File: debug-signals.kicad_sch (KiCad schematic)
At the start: 77 parts, among them U11 TCA9534PWR, U12 TCA9534PWR, U13 Si7021, U14 TCA9534PWR, U15 TCA9534PWR

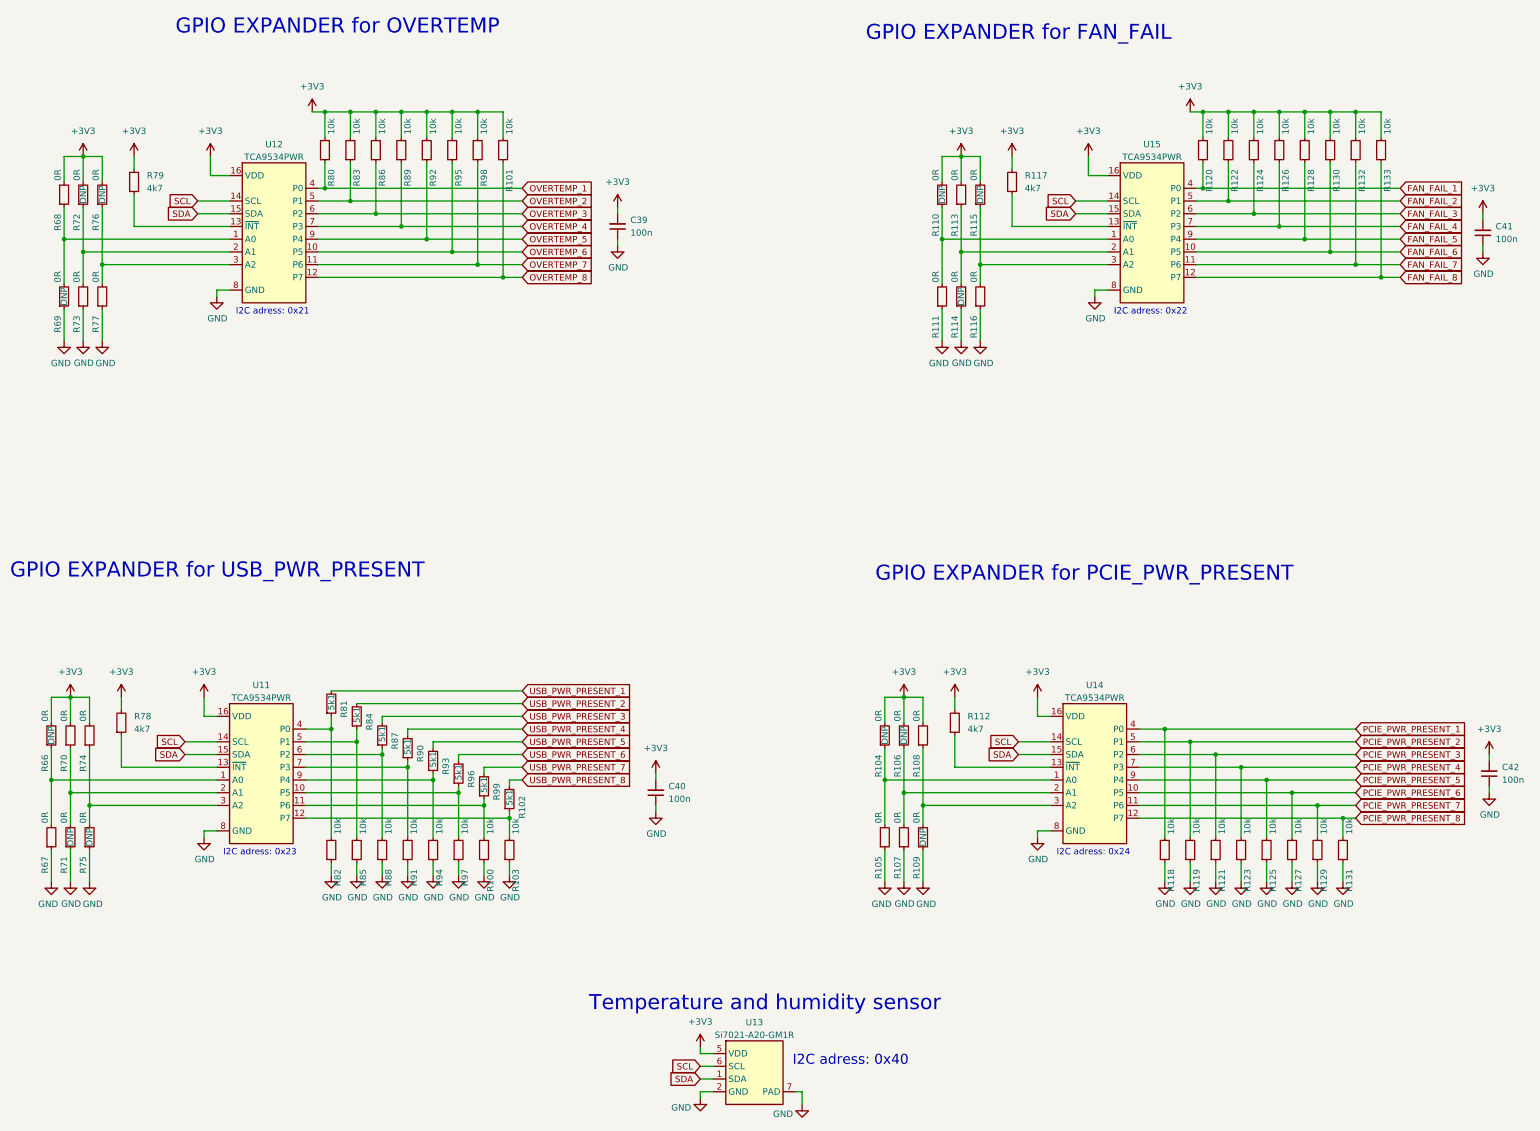
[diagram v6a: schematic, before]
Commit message: Minor fixes in schematic layout and reannotate
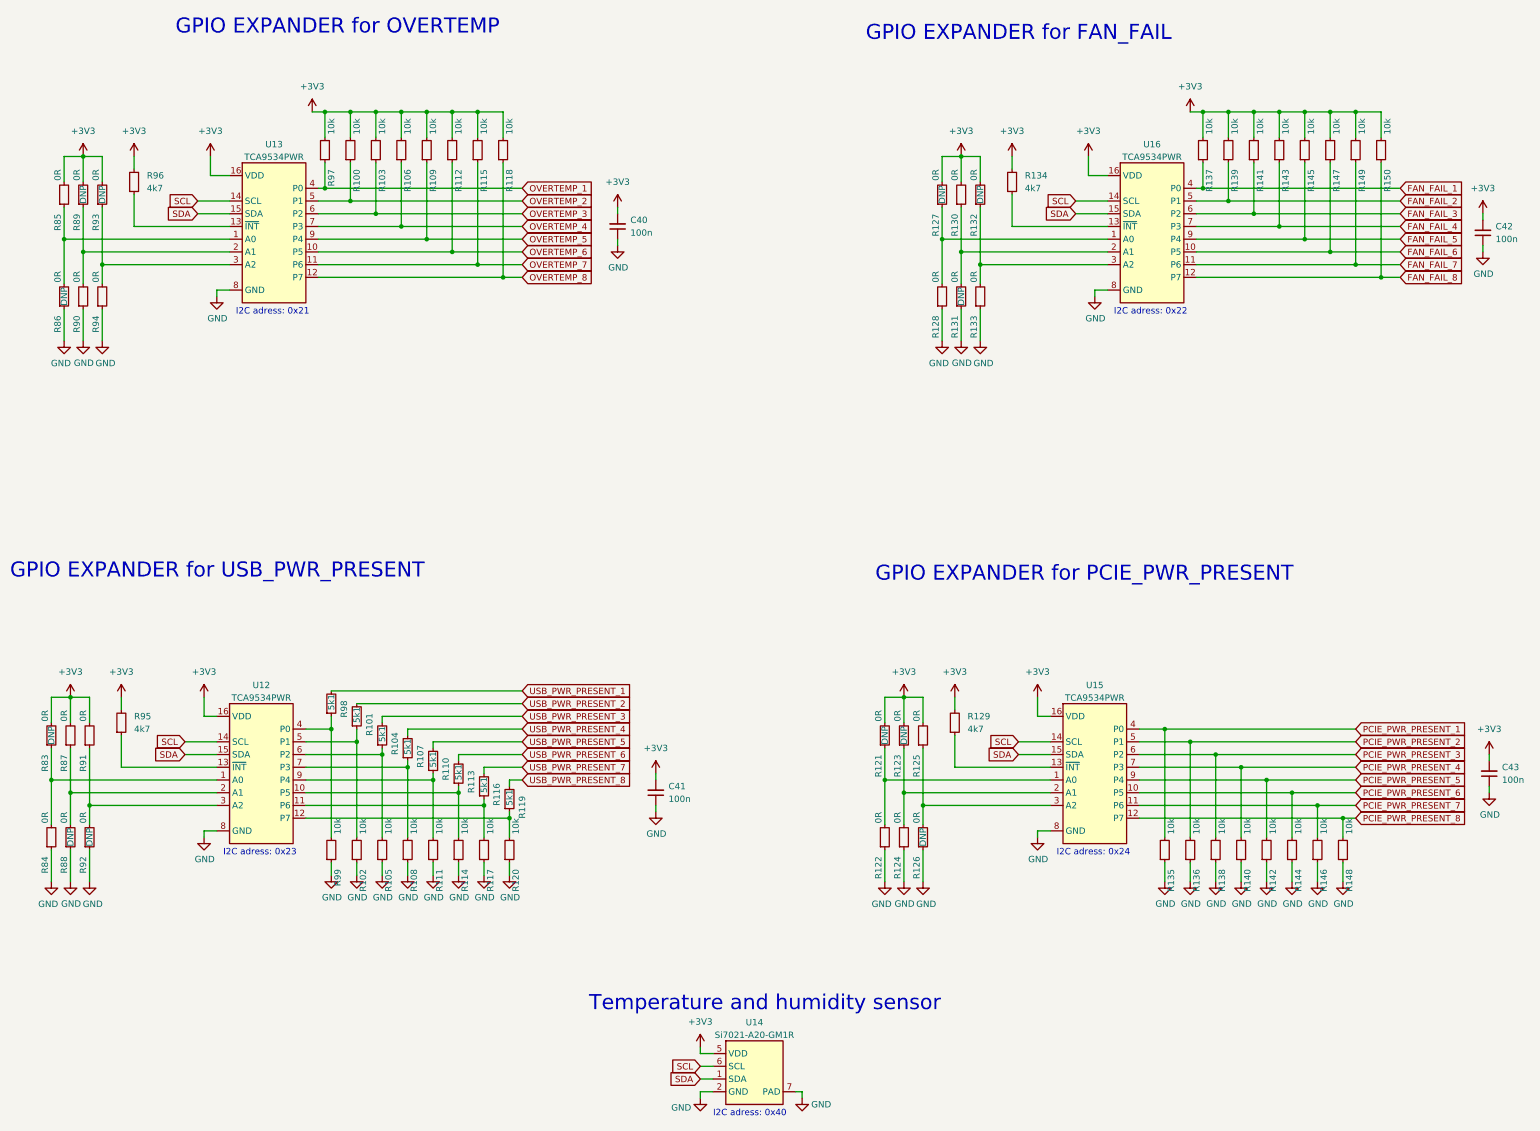
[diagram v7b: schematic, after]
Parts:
- renumbered C39 to C40, C40 to C41, C41 to C42, C42 to C43, R83 to R100, R84 to R101, R85 to R102, R86 to R103, R87 to R104, R88 to R105, R89 to R106, R90 to R107, R91 to R108, R92 to R109, R93 to R110, R94 to R111, R95 to R112, R96 to R113, R97 to R114, R98 to R115, R99 to R116, R100 to R117, R101 to R118, R102 to R119, R103 to R120, R104 to R121, R105 to R122, R106 to R123, R107 to R124, R108 to R125, R109 to R126, R110 to R127, R111 to R128, R112 to R129, R113 to R130, R114 to R131, R115 to R132, R116 to R133, R117 to R134, R118 to R135, R119 to R136, R120 to R137, R121 to R138, R122 to R139, R123 to R140, R124 to R141, R125 to R142, R126 to R143, R127 to R144, R128 to R145, R129 to R146, R130 to R147, R131 to R148, R132 to R149, R133 to R150, R66 to R83, R67 to R84, R68 to R85, R69 to R86, R70 to R87, R71 to R88, R72 to R89, R73 to R90, R74 to R91, R75 to R92, R76 to R93, R77 to R94, R78 to R95, R79 to R96, R80 to R97, R81 to R98, R82 to R99, U11 to U12, U12 to U13, U13 to U14, U14 to U15, U15 to U16
